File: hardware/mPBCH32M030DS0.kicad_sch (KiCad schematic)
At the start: 0 parts

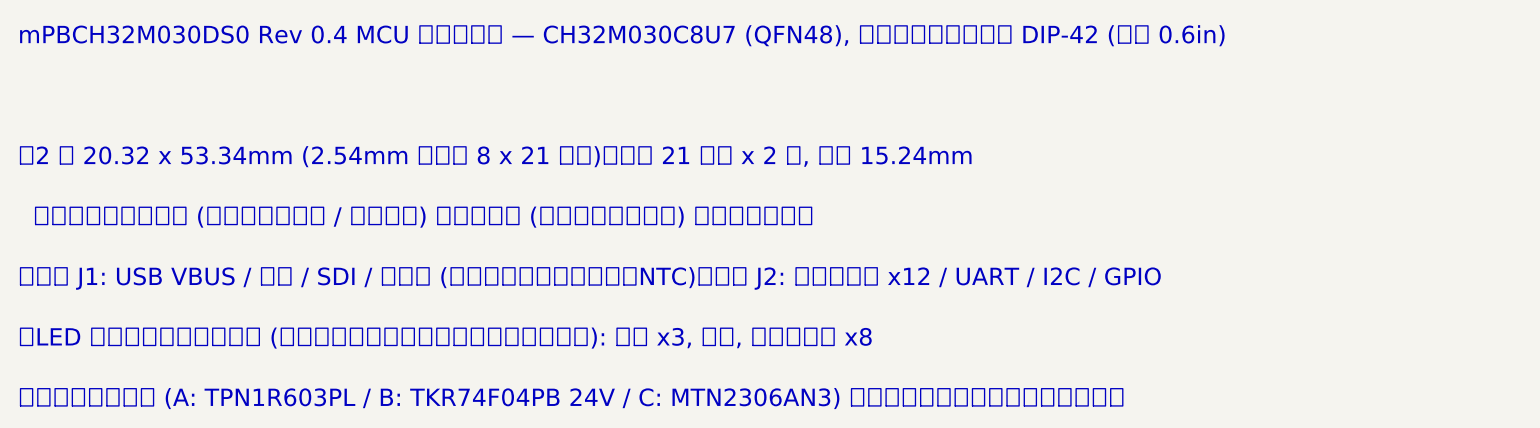
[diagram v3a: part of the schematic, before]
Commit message: 9マス版に一本化 (8マス版を削除)
- 8 マス版 (20.32mm) は JLCPCB の 2 層標準 0.127mm で配線しきれないため削除
- 9 マス版 (22.86mm, 端子列 0.7in) を hardware/ 直下・hardware/daughter/・hardware/fab/・docs/pcb/ へ移動
- ベタなし版は hardware/nopour/ (図は docs/pcb/nopour/)
- gen_pcb.py から MPB_W9 の切り替えを外し 9 マス固定に。既定ルールは 0.127mm / ビア 0.6/0.3
  (再生成した配置が確定済みの 4 基板と一致することを確認)
- 回路図の注記 (外形・列間) を 22.86mm / 17.78mm に更新し PDF を再出力
- README / stacking.md / design.md を 9 マス版のみの記述に更新

Co-Authored-By: Claude Opus 5.5 <noreply@anthropic.com>
Claude-Session: https://claude.ai/code/session_01LENFjjhDfYjJZV1NWhB9uV
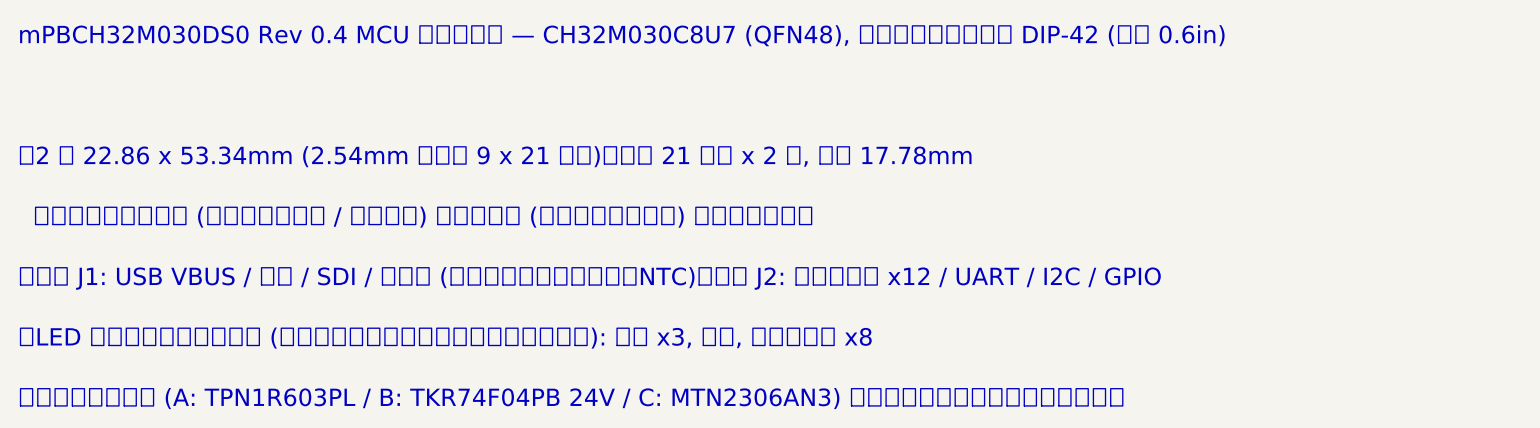
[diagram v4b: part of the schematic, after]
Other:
- note added: "・2 層 22.86 x 53.34mm (2.54mm 格子で 9 x 21 マス)。左右 21 ピン x 2 列, 列間 17.78mm"
- note removed: "・2 層 20.32 x 53.34mm (2.54mm 格子で 8 x 21 マス)。左右 21 ピン x 2 列, 列間 15.24mm"
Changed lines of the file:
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@@
 (text "mPBCH32M030DS0 Rev 0.4 MCU モジュール — CH32M030C8U7 (QFN48), ブレッドボード対応 DIP-42 (列間 0.6in)" (exclude_from_sim no) (at 20 30 0) (effects (font (size 2 2)) (justify left bottom)))
 (text "" (exclude_from_sim no) (at 20 37 0) (effects (font (size 2 2)) (justify left bottom)))
-(text "・2 層 20.32 x 53.34mm (2.54mm 格子で 8 x 21 マス)。左右 21 ピン x 2 列, 列間 15.24mm" (exclude_from_sim no) (at 20 44 0) (effects (font (size 2 2)) (justify left bottom)))
+(text "・2 層 22.86 x 53.34mm (2.54mm 格子で 9 x 21 マス)。左右 21 ピン x 2 列, 列間 17.78mm" (exclude_from_sim no) (at 20 44 0) (effects (font (size 2 2)) (justify left bottom)))
 (text "  ピンヘッダは裏から (ブレッドボード / 子基板用) でも表から (ジャンパワイヤ用) でも実装できる" (exclude_from_sim no) (at 20 51 0) (effects (font (size 2 2)) (justify left bottom)))
 (text "・左列 J1: USB VBUS / 電源 / SDI / センサ (相電圧・ホール・電流・NTC)。右列 J2: ゲート駆動 x12 / UART / I2C / GPIO" (exclude_from_sim no) (at 20 58 0) (effects (font (size 2 2)) (justify left bottom)))
